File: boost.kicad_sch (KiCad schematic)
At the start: 25 parts, among them Q3 BSC059N04LS6, Q4 BSC059N04LS6, U7 LTC7804

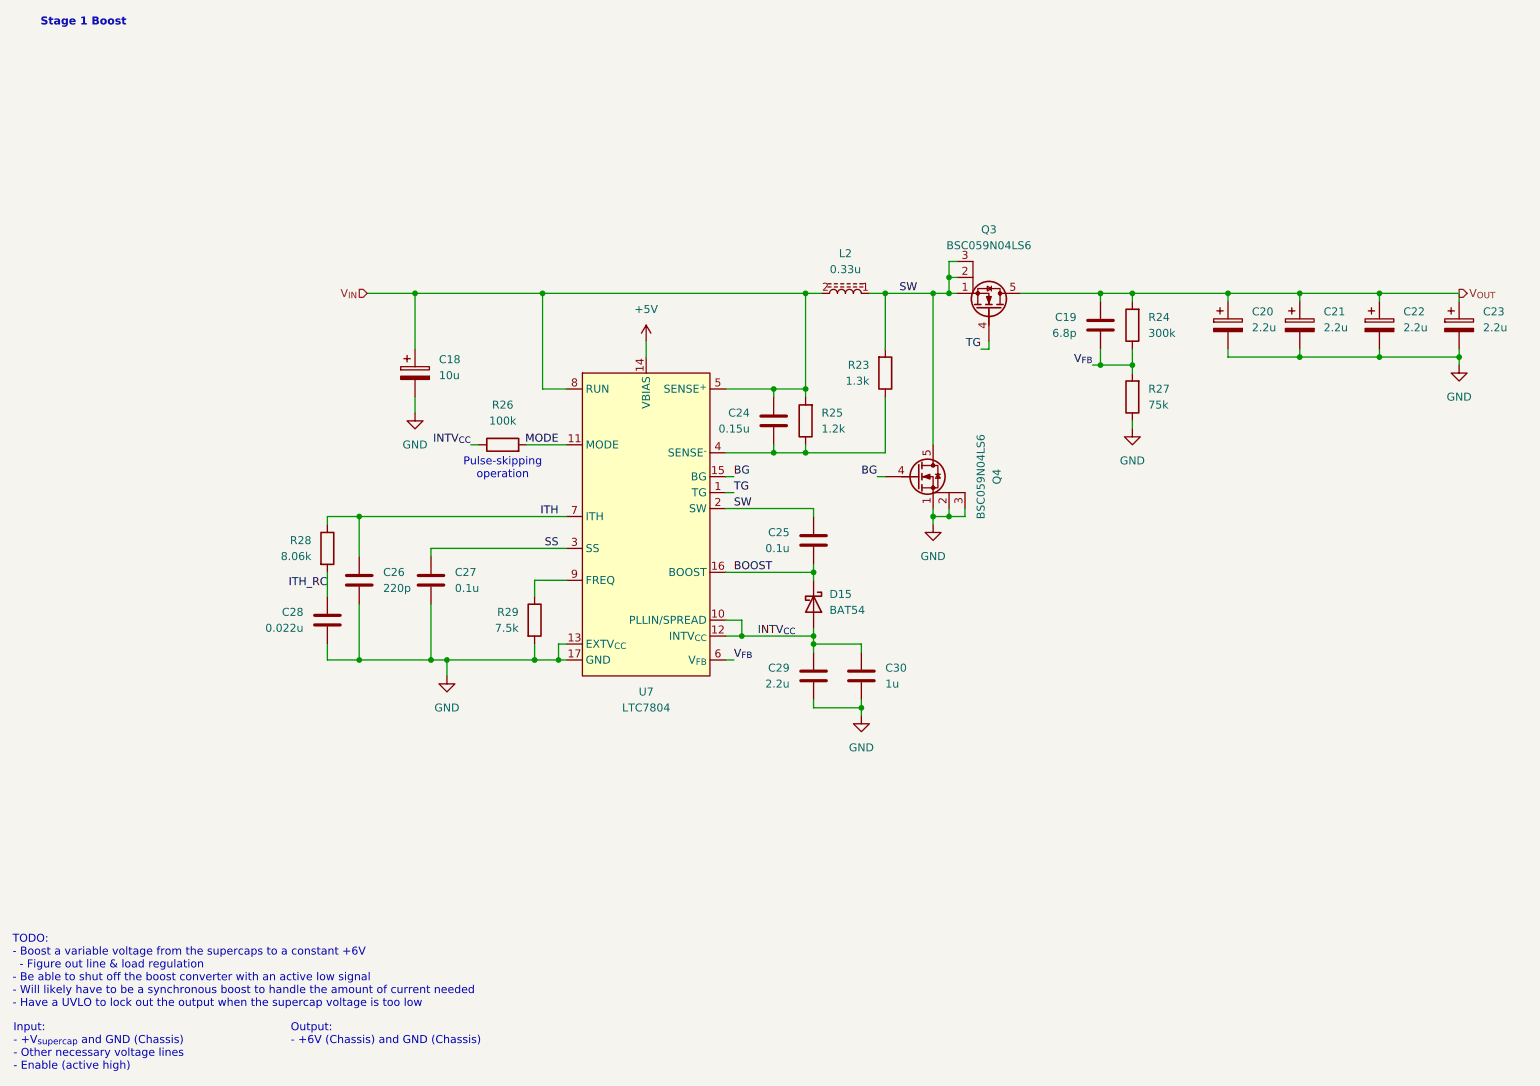
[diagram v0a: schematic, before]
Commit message: Tuned circuits & adjusted values
Changed footprints for some circuits to consolidate components
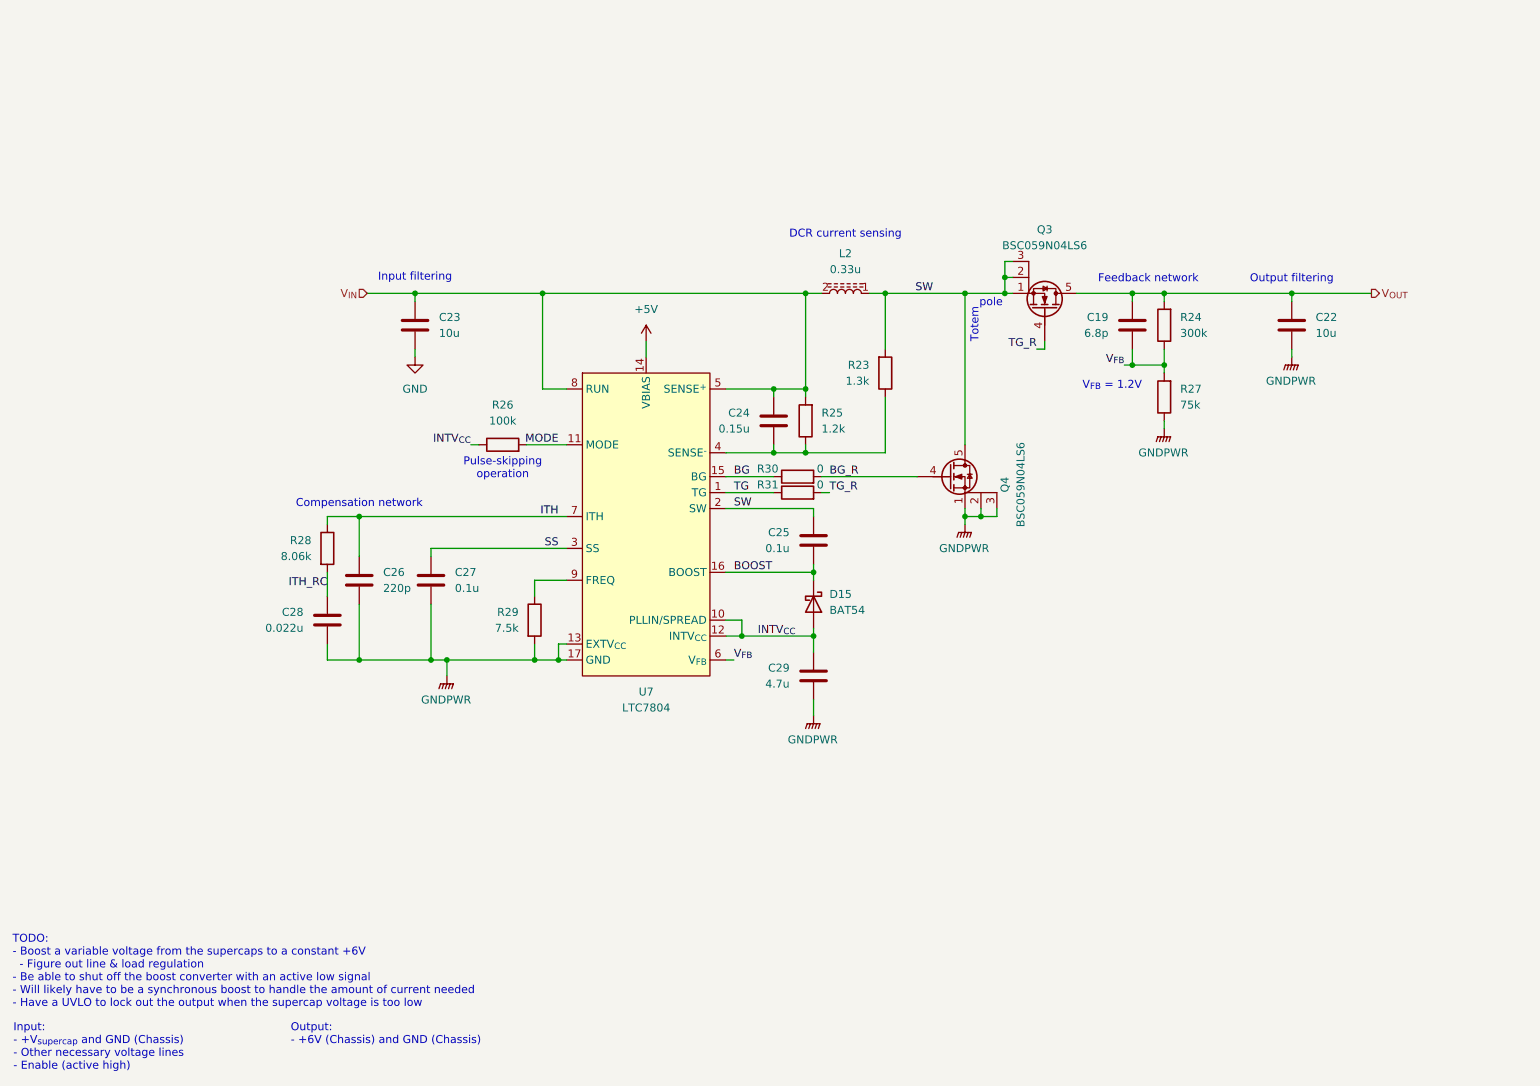
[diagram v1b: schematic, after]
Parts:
- removed C18: 10u, Capacitor_THT:CP_Radial_D5.0mm_P2.00mm, symbol Device:C_Polarized
- removed C20, C21, C22, C23: 2.2u, Capacitor_THT:CP_Radial_D5.0mm_P2.00mm, symbol Device:C_Polarized
- removed C30: 1u, Capacitor_SMD:C_0603_1608Metric_Pad1.08x0.95mm_HandSolder, symbol Device:C
- added C22, C23: 10u, Capacitor_SMD:C_0805_2012Metric_Pad1.18x1.45mm_HandSolder, symbol Device:C
- added R30, R31: 0, Resistor_SMD:R_0603_1608Metric_Pad0.98x0.95mm_HandSolder, symbol Device:R
- C29: value 2.2u -> 4.7u
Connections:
- net BG: now also R30.1; no longer Q4.4 (G)
- net GND: now also C23.2; no longer C26.2, C27.2, C28.2, C29.2, Q4.1 (S), Q4.2 (S), Q4.3 (S), R27.1, R29.2, U7.13 (EXTV_{CC}), U7.17 (GND)
- net TG: now also R31.1; no longer Q3.4 (G)
- net V_{IN}: now also C23.1
- net V_{OUT}: now also C22.1
- new net BG_R: Q4.4 (G), R30.2
- new net GNDPWR: C22.2, C26.2, C27.2, C28.2, C29.2, Q4.1 (S), Q4.2 (S), Q4.3 (S), R27.1, R29.2, U7.13 (EXTV_{CC}), U7.17 (GND)
- new net TG_R: Q3.4 (G), R31.2
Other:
- note added: "Compensation network"
- note added: "DCR current sensing"
- note added: "Feedback network"
- note added: "Input filtering"
- note added: "Output filtering"
- note added: "Totem"
- note added: "V_{FB} = 1.2V"
- note added: "pole"
- note removed: "Stage 1 Boost"
- moved on the sheet: C19, Q3, Q4, R24, R27

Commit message: Considering using a different IC for 1st stage
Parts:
- added C64: 1u, Capacitor_SMD:C_0603_1608Metric_Pad1.08x0.95mm_HandSolder, symbol Device:C
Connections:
- net +5V is gone; now on net V_{OUT}: U7.14 (VBIAS)
- net GNDPWR: now also C64.2; no longer U7.13 (EXTV_{CC})
- net INTV_{CC}: now also C64.1
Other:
- moved on the sheet: C29

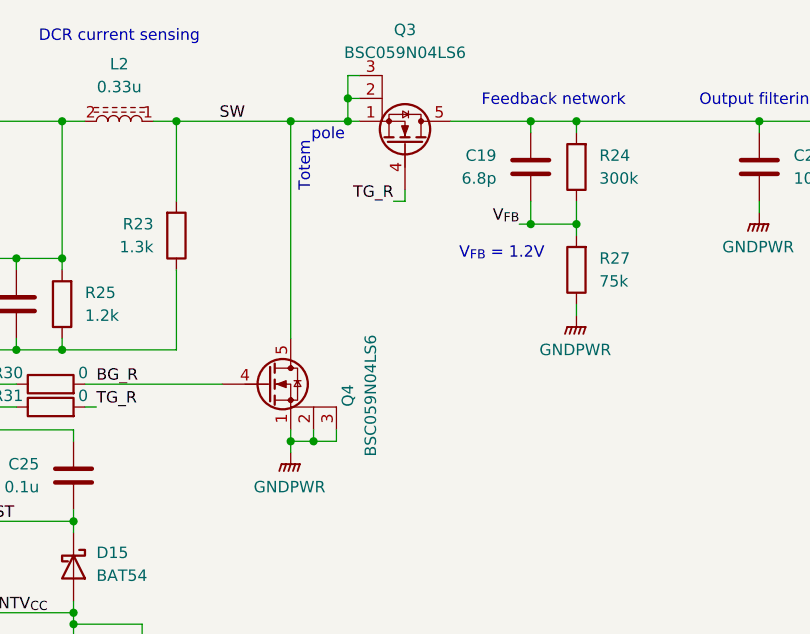
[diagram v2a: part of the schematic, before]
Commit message: Redesigning output boosts to be more efficient albeit with less current capacity
idk what I changed with the schematics lol
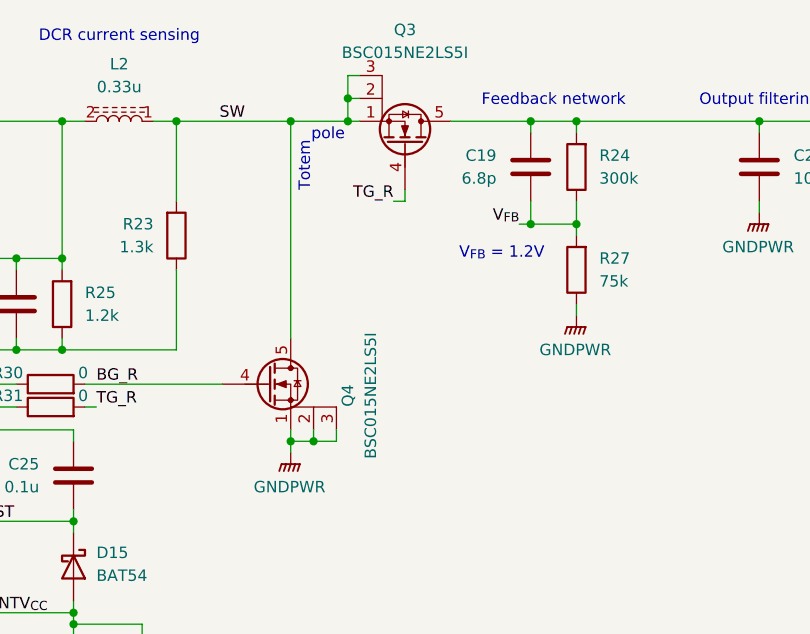
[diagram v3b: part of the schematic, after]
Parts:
- Q3, Q4: value BSC059N04LS6 -> BSC015NE2LS5I; Mouser Part Number 726-BSC059N04LS6ATMA -> 726-BSC015NE2LS5IATM
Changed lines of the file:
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@@
 			)
 		)
-		(property "Value" "BSC059N04LS6"
+		(property "Value" "BSC015NE2LS5I"
 			(at 180.34 97.79 90)
 			(effects
@@
 			)
 		)
-		(property "Datasheet" "https://www.mouser.com/datasheet/2/196/Infineon_BSC059N04LS6_DataSheet_v02_01_EN-3360636.pdf"
+		(property "Datasheet" "https://www.mouser.com/datasheet/2/196/Infineon_BSC015NE2LS5I_DataSheet_v02_01_EN-3360635.pdf"
 			(at 168.91 96.52 0)
 			(effects
@@
 			)
 		)
-		(property "Mouser Part Number" "726-BSC059N04LS6ATMA"
+		(property "Mouser Part Number" "726-BSC015NE2LS5IATM"
 			(at 168.91 96.52 0)
 			(effects
@@
 			)
 		)
-		(property "Value" "BSC059N04LS6"
+		(property "Value" "BSC015NE2LS5I"
 			(at 184.15 59.69 90)
 			(effects
@@
 			)
 		)
-		(property "Datasheet" "https://www.mouser.com/datasheet/2/196/Infineon_BSC059N04LS6_DataSheet_v02_01_EN-3360636.pdf"
+		(property "Datasheet" "https://www.mouser.com/datasheet/2/196/Infineon_BSC015NE2LS5I_DataSheet_v02_01_EN-3360635.pdf"
 			(at 184.15 69.85 0)
 			(effects
@@
 			)
 		)
-		(property "Mouser Part Number" "726-BSC059N04LS6ATMA"
+		(property "Mouser Part Number" "726-BSC015NE2LS5IATM"
 			(at 184.15 69.85 0)
 			(effects

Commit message: Up charging current to 6A
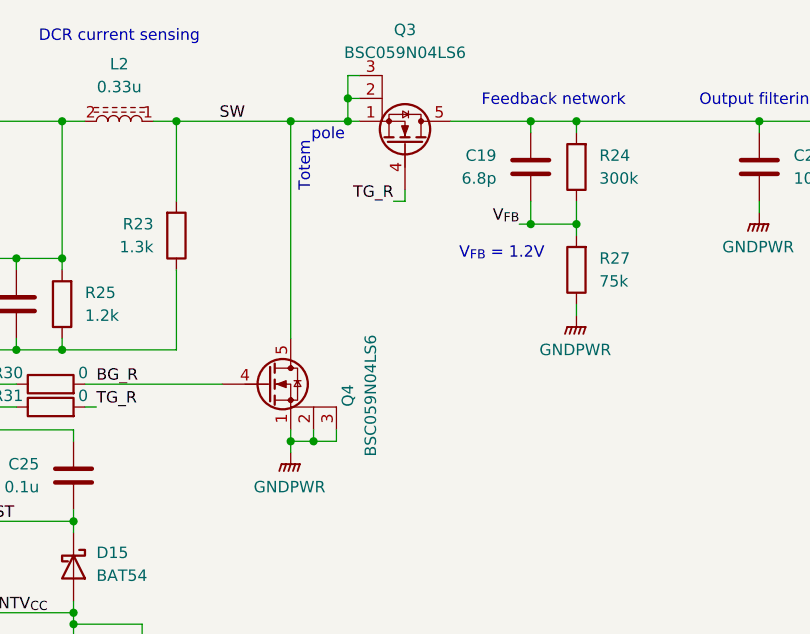
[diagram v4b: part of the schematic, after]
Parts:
- Q3, Q4: value BSC015NE2LS5I -> BSC059N04LS6; Mouser Part Number 726-BSC015NE2LS5IATM -> 726-BSC059N04LS6ATMA
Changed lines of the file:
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@@
 			)
 		)
-		(property "Value" "BSC015NE2LS5I"
+		(property "Value" "BSC059N04LS6"
 			(at 180.34 97.79 90)
 			(effects
@@
 			)
 		)
-		(property "Mouser Part Number" "726-BSC015NE2LS5IATM"
+		(property "Mouser Part Number" "726-BSC059N04LS6ATMA"
 			(at 168.91 96.52 0)
 			(effects
@@
 			)
 		)
-		(property "Value" "BSC015NE2LS5I"
+		(property "Value" "BSC059N04LS6"
 			(at 184.15 59.69 90)
 			(effects
@@
 			)
 		)
-		(property "Mouser Part Number" "726-BSC015NE2LS5IATM"
+		(property "Mouser Part Number" "726-BSC059N04LS6ATMA"
 			(at 184.15 69.85 0)
 			(effects
